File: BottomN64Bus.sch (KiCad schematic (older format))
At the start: 3 parts

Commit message: Add reference
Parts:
- P4: renamed from J?; value Conn_02x25_N64_Cartridge -> N64_Cartridge_Edge
- gave numbers to parts that had none: 2
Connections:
- wire segments 0 -> 57
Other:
- moved on the sheet: P4
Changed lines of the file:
@@
 $Descr A4 11693 8268
 encoding utf-8
-Sheet 7 7
+Sheet 5 8
 Title "Rare N64DEV V3 - Bottom N64 Bus"
 Date "2021-12-30"
@@
 $EndDescr
 $Comp
-L N64DEV:Conn_02x25_N64_Cartridge J?
+L N64DEV:Conn_02x25_N64_Cartridge P4
 U 1 1 61D8F3A5
-P 5850 3600
-F 0 "J?" H 5900 5017 50  0000 C CNN
-F 1 "Conn_02x25_N64_Cartridge" H 5900 4926 50  0000 C CNN
-F 2 "" H 5850 3600 50  0001 C CNN
-F 3 "~" H 5850 3600 50  0001 C CNN
-	1    5850 3600
+P 5950 3750
+F 0 "P4" H 6000 5167 50  0000 C CNN
+F 1 "N64_Cartridge_Edge" H 6000 5076 50  0000 C CNN
+F 2 "" H 5950 3750 50  0001 C CNN
+F 3 "~" H 5950 3750 50  0001 C CNN
+	1    5950 3750
 	1    0    0    -1
 $EndComp
 $Comp
-L N64DEV:BU9850_BK16D U?
+L N64DEV:BU9850_BK16D U21
 U 1 1 61D90EA1
 P 4050 2850
-F 0 "U?" H 4050 3431 50  0000 C CNN
-F 1 "BU9850_BK16D" H 4050 3340 50  0000 C CNN
+F 0 "U21" H 3800 3100 50  0000 C CNN
+F 1 "BU9850_BK16D" H 4400 2600 50  0000 C CNN
 F 2 "Package_DIP:DIP-8_W7.62mm_Socket" H 4050 2850 50  0001 C CNN
 F 3 "" H 4050 2850 50  0001 C CNN
@@
 $EndComp
 $Comp
-L N64DEV:CIC-NUS-xxxx U?
+L N64DEV:CIC-NUS-xxxx U23
 U 1 1 61D912D2
 P 4100 4500
-F 0 "U?" H 4100 5081 50  0000 C CNN
-F 1 "CIC-NUS-xxxx" H 4100 4990 50  0000 C CNN
+F 0 "U23" H 3850 4750 50  0000 C CNN
+F 1 "CIC-NUS-xxxx" H 4450 4250 50  0000 C CNN
 F 2 "Package_DIP:DIP-16_W7.62mm_Socket" H 4100 4500 50  0001 C CNN
 F 3 "" H 4100 4500 50  0001 C CNN
@@
 	1    0    0    -1
 $EndComp
+Wire Wire Line
+	6250 2550 6500 2550
+Wire Wire Line
+	6250 2650 6500 2650
+Wire Wire Line
+	6250 2750 6500 2750
+Wire Wire Line
+	6250 2850 6500 2850
+Wire Wire Line
+	6250 2950 6500 2950
+Wire Wire Line
+	6250 3050 6500 3050
+Wire Wire Line
+	6250 3150 6500 3150
+Wire Wire Line
+	6250 3250 6500 3250
+Wire Wire Line
+	6250 3350 6500 3350
+Wire Wire Line
+	6250 3450 6500 3450
+Wire Wire Line
+	6250 3550 6500 3550
+Wire Wire Line
+	6250 3650 6500 3650
+Wire Wire Line
+	6250 3750 6500 3750
+Wire Wire Line
+	6250 3850 6500 3850
+Wire Wire Line
+	6250 3950 6500 3950
+Wire Wire Line
+	6250 4050 6500 4050
+Wire Wire Line
+	6250 4150 6500 4150
+Wire Wire Line
+	6250 4250 6500 4250
+Wire Wire Line
+	6250 4350 6500 4350
+Wire Wire Line
+	6250 4450 6500 4450
+Wire Wire Line
+	6250 4550 6500 4550
+Wire Wire Line
+	6250 4650 6500 4650
+Wire Wire Line
+	6250 4750 6500 4750
+Wire Wire Line
+	6250 4850 6500 4850
+Wire Wire Line
+	6250 4950 6500 4950
+Wire Wire Line
+	5750 2950 5500 2950
+Wire Wire Line
+	5750 2850 5500 2850
+Wire Wire Line
+	5750 2750 5500 2750
+Wire Wire Line
+	5750 2650 5500 2650
+Wire Wire Line
+	5750 2550 5500 2550
+Wire Wire Line
+	5750 3450 5500 3450
+Wire Wire Line
+	5750 3350 5500 3350
+Wire Wire Line
+	5750 3250 5500 3250
+Wire Wire Line
+	5750 3150 5500 3150
+Wire Wire Line
+	5750 3050 5500 3050
+Wire Wire Line
+	5750 3950 5500 3950
+Wire Wire Line
+	5750 3850 5500 3850
+Wire Wire Line
+	5750 3750 5500 3750
+Wire Wire Line
+	5750 3650 5500 3650
+Wire Wire Line
+	5750 3550 5500 3550
+Wire Wire Line
+	5750 4450 5500 4450
+Wire Wire Line
+	5750 4350 5500 4350
+Wire Wire Line
+	5750 4250 5500 4250
+Wire Wire Line
+	5750 4150 5500 4150
+Wire Wire Line
+	5750 4050 5500 4050
+Wire Wire Line
+	5750 4950 5500 4950
+Wire Wire Line
+	5750 4850 5500 4850
+Wire Wire Line
+	5750 4750 5500 4750
+Wire Wire Line
+	5750 4650 5500 4650
+Wire Wire Line
+	5750 4550 5500 4550
+Wire Wire Line
+	4550 2750 4800 2750
+Wire Wire Line
+	4550 2850 4800 2850
+Wire Wire Line
+	4600 4400 4850 4400
+Wire Wire Line
+	4600 4500 4850 4500
+Wire Wire Line
+	4600 4600 4850 4600
+Wire Wire Line
+	3350 4400 3600 4400
+Wire Wire Line
+	3300 2750 3550 2750
 $EndSCHEMATC

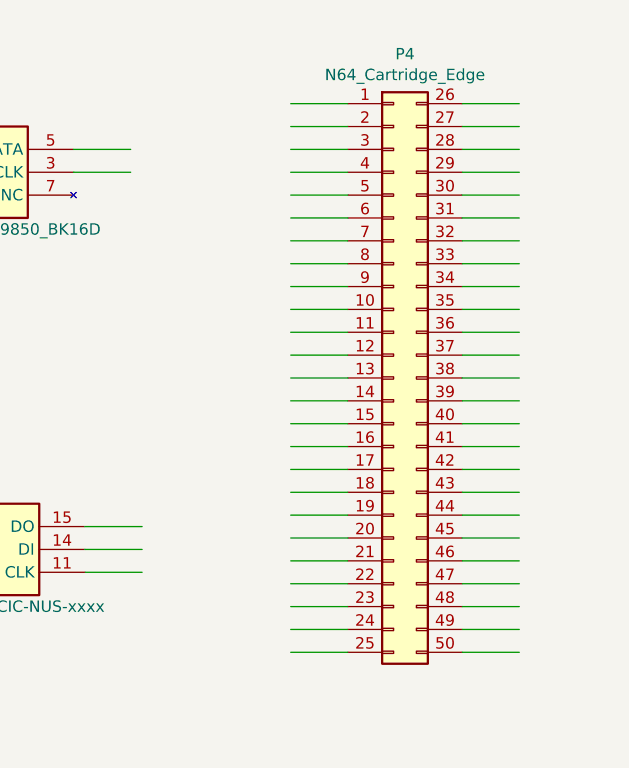
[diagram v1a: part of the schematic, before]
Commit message: Add N64 edge net name
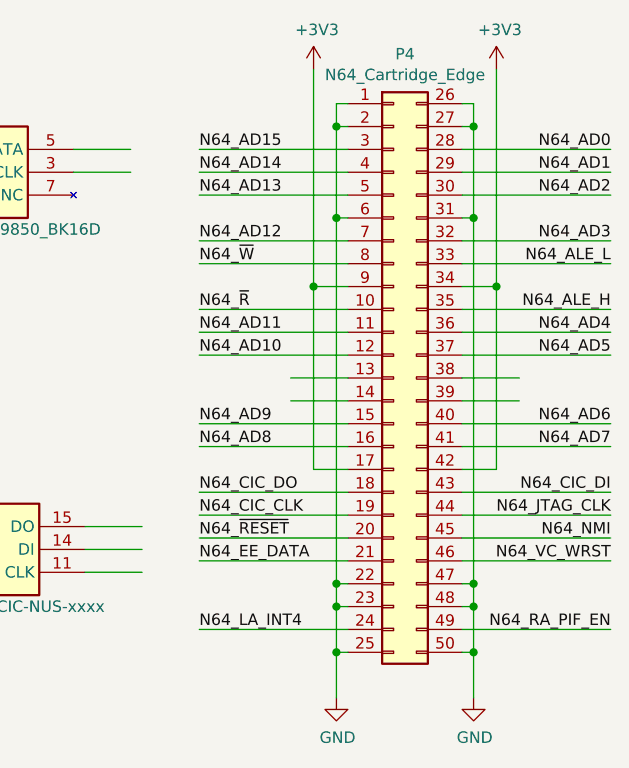
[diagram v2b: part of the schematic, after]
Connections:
- net labels added: +3V3, GND, N64_AD0, N64_AD1, N64_AD10, N64_AD11, N64_AD12, N64_AD13, N64_AD14, N64_AD15, N64_AD2, N64_AD3, N64_AD4, N64_AD5, N64_AD6, N64_AD7, N64_AD8, N64_AD9, N64_ALE_H, N64_ALE_L, N64_CIC_CLK, N64_CIC_DI, N64_CIC_DO, N64_EE_DATA, N64_JTAG_CLK, N64_LA_INT4, N64_NMI, N64_RA_PIF_EN, N64_VC_WRST, N64_~RESET~, N64_~R~, N64_~W~
- wire segments 57 -> 73
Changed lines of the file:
@@
 $EndComp
-Wire Wire Line
-	6250 2550 6500 2550
-Wire Wire Line
-	6250 2650 6500 2650
-Wire Wire Line
-	6250 2750 6500 2750
-Wire Wire Line
-	6250 2850 6500 2850
-Wire Wire Line
-	6250 2950 6500 2950
-Wire Wire Line
-	6250 3050 6500 3050
-Wire Wire Line
-	6250 3150 6500 3150
-Wire Wire Line
-	6250 3250 6500 3250
-Wire Wire Line
-	6250 3350 6500 3350
-Wire Wire Line
-	6250 3450 6500 3450
-Wire Wire Line
-	6250 3550 6500 3550
-Wire Wire Line
-	6250 3650 6500 3650
 Wire Wire Line
 	6250 3750 6500 3750
@@
 	6250 3850 6500 3850
 Wire Wire Line
-	6250 3950 6500 3950
-Wire Wire Line
-	6250 4050 6500 4050
-Wire Wire Line
-	6250 4150 6500 4150
-Wire Wire Line
-	6250 4250 6500 4250
-Wire Wire Line
-	6250 4350 6500 4350
-Wire Wire Line
-	6250 4450 6500 4450
-Wire Wire Line
-	6250 4550 6500 4550
-Wire Wire Line
-	6250 4650 6500 4650
-Wire Wire Line
-	6250 4750 6500 4750
-Wire Wire Line
-	6250 4850 6500 4850
-Wire Wire Line
-	6250 4950 6500 4950
-Wire Wire Line
-	5750 2950 5500 2950
-Wire Wire Line
-	5750 2850 5500 2850
-Wire Wire Line
-	5750 2750 5500 2750
-Wire Wire Line
-	5750 2650 5500 2650
-Wire Wire Line
-	5750 2550 5500 2550
-Wire Wire Line
-	5750 3450 5500 3450
-Wire Wire Line
-	5750 3350 5500 3350
-Wire Wire Line
-	5750 3250 5500 3250
-Wire Wire Line
-	5750 3150 5500 3150
-Wire Wire Line
-	5750 3050 5500 3050
-Wire Wire Line
-	5750 3950 5500 3950
-Wire Wire Line
 	5750 3850 5500 3850
 Wire Wire Line
 	5750 3750 5500 3750
 Wire Wire Line
-	5750 3650 5500 3650
-Wire Wire Line
-	5750 3550 5500 3550
-Wire Wire Line
-	5750 4450 5500 4450
-Wire Wire Line
-	5750 4350 5500 4350
-Wire Wire Line
-	5750 4250 5500 4250
-Wire Wire Line
-	5750 4150 5500 4150
-Wire Wire Line
-	5750 4050 5500 4050
-Wire Wire Line
-	5750 4950 5500 4950
-Wire Wire Line
-	5750 4850 5500 4850
-Wire Wire Line
-	5750 4750 5500 4750
-Wire Wire Line
-	5750 4650 5500 4650
-Wire Wire Line
-	5750 4550 5500 4550
-Wire Wire Line
 	4550 2750 4800 2750
 Wire Wire Line
@@
 Wire Wire Line
 	3300 2750 3550 2750
+$Comp
+L N64DEV:GND #PWR?
+U 1 1 62663AC3
+P 5700 5150
+F 0 "#PWR?" H 5700 4900 50  0001 C CNN
+F 1 "GND" H 5705 4977 50  0000 C CNN
+F 2 "" H 5700 5150 50  0001 C CNN
+F 3 "" H 5700 5150 50  0001 C CNN
+	1    5700 5150
+	1    0    0    -1
+$EndComp
+Wire Wire Line
+	6250 2550 6300 2550
+$Comp
+L N64DEV:GND #PWR?
+U 1 1 6266A81A
+P 6300 5150
+F 0 "#PWR?" H 6300 4900 50  0001 C CNN
+F 1 "GND" H 6305 4977 50  0000 C CNN
+F 2 "" H 6300 5150 50  0001 C CNN
+F 3 "" H 6300 5150 50  0001 C CNN
+	1    6300 5150
+	1    0    0    -1
+$EndComp
+Wire Wire Line
+	6250 2650 6300 2650
+Wire Wire Line
+	6250 4650 6300 4650
+Wire Wire Line
+	6250 4750 6300 4750
+Wire Wire Line
+	6250 4950 6300 4950
+Wire Wire Line
+	6250 3050 6300 3050
+$Comp
+L N64DEV:+3V3 #PWR?
+U 1 1 6267DD96
+P 5600 2400
+F 0 "#PWR?" H 5600 2250 50  0001 C CNN
+F 1 "+3V3" H 5615 2573 50  0000 C CNN
+F 2 "" H 5600 2400 50  0001 C CNN
+F 3 "" H 5600 2400 50  0001 C CNN
+	1    5600 2400
+	1    0    0    -1
+$EndComp
+Wire Wire Line
+	5600 3350 5600 2400
+Wire Wire Line
+	5600 3350 5750 3350
+$Comp
+L N64DEV:+3V3 #PWR?
+U 1 1 6268071B
+P 6400 2400
+F 0 "#PWR?" H 6400 2250 50  0001 C CNN
+F 1 "+3V3" H 6415 2573 50  0000 C CNN
+F 2 "" H 6400 2400 50  0001 C CNN
+F 3 "" H 6400 2400 50  0001 C CNN
+	1    6400 2400
+	1    0    0    -1
+$EndComp
+Wire Wire Line
+	6400 3350 6400 2400
+Wire Wire Line
+	6250 3350 6400 3350
+Wire Wire Line
+	5600 4150 5600 3350
+Wire Wire Line
+	5600 4150 5750 4150
+Connection ~ 5600 3350
+Wire Wire Line
+	6400 4150 6400 3350
+Wire Wire Line
+	6250 4150 6400 4150
+Connection ~ 6400 3350
+Text Label 5100 2750 0    50   ~ 0
+N64_AD15
+Text Label 5100 2850 0    50   ~ 0
+N64_AD14
+Text Label 5100 2950 0    50   ~ 0
+N64_AD13
+Text Label 5100 3150 0    50   ~ 0
+N64_AD12
+Text Label 5100 3250 0    50   ~ 0
+N64_~W~
+Text Label 5100 3450 0    50   ~ 0
+N64_~R~
+Text Label 5100 3550 0    50   ~ 0
+N64_AD11
+Text Label 5100 3650 0    50   ~ 0
+N64_AD10
+Text Label 5100 3950 0    50   ~ 0
+N64_AD9
+Text Label 5100 4050 0    50   ~ 0
+N64_AD8
+Text Label 5100 4250 0    50   ~ 0
+N64_CIC_DO
+Text Label 5100 4350 0    50   ~ 0
+N64_CIC_CLK
+Text Label 5100 4450 0    50   ~ 0
+N64_~RESET~
+Text Label 5100 4550 0    50   ~ 0
+N64_EE_DATA
+Text Label 5100 4850 0    50   ~ 0
+N64_LA_INT4
+Text Label 6900 4850 2    50   ~ 0
+N64_RA_PIF_EN
+Text Label 6900 4550 2    50   ~ 0
+N64_VC_WRST
+Text Label 6900 4450 2    50   ~ 0
+N64_NMI
+Text Label 6900 4350 2    50   ~ 0
+N64_JTAG_CLK
+Text Label 6900 4250 2    50   ~ 0
+N64_CIC_DI
+Text Label 6900 4050 2    50   ~ 0
+N64_AD7
+Text Label 6900 3950 2    50   ~ 0
+N64_AD6
+Text Label 6900 3650 2    50   ~ 0
+N64_AD5
+Text Label 6900 3550 2    50   ~ 0
+N64_AD4
+Text Label 6900 3450 2    50   ~ 0
+N64_ALE_H
+Text Label 6900 3150 2    50   ~ 0
+N64_AD3
+Text Label 6900 3250 2    50   ~ 0
+N64_ALE_L
+Text Label 6900 2950 2    50   ~ 0
+N64_AD2
+Text Label 6900 2850 2    50   ~ 0
+N64_AD1
+Text Label 6900 2750 2    50   ~ 0
+N64_AD0
+Wire Wire Line
+	5700 2550 5700 2650
+Wire Wire Line
+	5700 2550 5750 2550
+Connection ~ 5700 2650
+Wire Wire Line
+	5700 2650 5750 2650
+Wire Wire Line
+	5700 2650 5700 3050
+Connection ~ 5700 3050
+Wire Wire Line
+	5700 3050 5750 3050
+Wire Wire Line
+	5700 3050 5700 4650
+Connection ~ 5700 4650
+Wire Wire Line
+	5700 4650 5750 4650
+Wire Wire Line
+	5700 4650 5700 4750
+Wire Wire Line
+	5700 4750 5750 4750
+Wire Wire Line
+	5700 4950 5700 5150
+Wire Wire Line
+	5700 4950 5750 4950
+Wire Wire Line
+	6300 2650 6300 2550
+Connection ~ 6300 2650
+Wire Wire Line
+	6300 2650 6300 3050
+Connection ~ 6300 3050
+Wire Wire Line
+	6300 4650 6300 4750
+Connection ~ 6300 4650
+Connection ~ 6300 4750
+Wire Wire Line
+	6300 4950 6300 5150
+Connection ~ 6300 4950
+Wire Wire Line
+	6300 4950 6300 4750
+Wire Wire Line
+	6300 4650 6300 3050
+Wire Wire Line
+	5700 4750 5700 4950
+Connection ~ 5700 4750
+Connection ~ 5700 4950
+Wire Wire Line
+	5100 2750 5750 2750
+Wire Wire Line
+	5100 2850 5750 2850
+Wire Wire Line
+	5100 2950 5750 2950
+Wire Wire Line
+	5100 3150 5750 3150
+Wire Wire Line
+	5100 3250 5750 3250
+Wire Wire Line
+	5100 3450 5750 3450
+Wire Wire Line
+	5100 3550 5750 3550
+Wire Wire Line
+	5100 3650 5750 3650
+Wire Wire Line
+	5100 3950 5750 3950
+Wire Wire Line
+	5100 4050 5750 4050
+Wire Wire Line
+	5100 4250 5750 4250
+Wire Wire Line
+	5100 4350 5750 4350
+Wire Wire Line
+	5100 4450 5750 4450
+Wire Wire Line
+	5100 4550 5750 4550
+Wire Wire Line
+	5100 4850 5750 4850
+Wire Wire Line
+	6250 4850 6900 4850
+Wire Wire Line
+	6250 4550 6900 4550
+Wire Wire Line
+	6250 4450 6900 4450
+Wire Wire Line
+	6250 4350 6900 4350
+Wire Wire Line
+	6250 4250 6900 4250
+Wire Wire Line
+	6250 4050 6900 4050
+Wire Wire Line
+	6250 3950 6900 3950
+Wire Wire Line
+	6250 3650 6900 3650
+Wire Wire Line
+	6250 3550 6900 3550
+Wire Wire Line
+	6250 3450 6900 3450
+Wire Wire Line
+	6250 3250 6900 3250
+Wire Wire Line
+	6250 3150 6900 3150
+Wire Wire Line
+	6250 2950 6900 2950
+Wire Wire Line
+	6250 2850 6900 2850
+Wire Wire Line
+	6250 2750 6900 2750
 $EndSCHEMATC

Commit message: MCU start
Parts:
- added C62, C63, C64, C65, C68: ~, symbol N64DEV:C_Small
- added C69: 10u, symbol N64DEV:CP1_Small
- added R28, R29, R30, R31: 4K7, symbol N64DEV:R_Small_US
- added R38, R39, R40, R41: 33, symbol N64DEV:R_Small_US
- added RP8, RP9: QSP16J-1-330, Package_SO:SSOP-16_3.9x4.9mm_P0.635mm, symbol N64DEV:QSP16J
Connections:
- net labels added: +12V, N64_PIF_CLK
- net labels removed: N64_CIC_CLK
- wire segments 73 -> 97
- no-connect marks 0 -> 2
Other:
- note added: "JTAG CLK trace was going to EEPROM socket pin 2.\nHowever the trace is manualy cut right over the P4."
- note added: "LA, RA, VC likely KMC equivalent signal (same pinout?)"
- moved on the sheet: P4, U21, U23
